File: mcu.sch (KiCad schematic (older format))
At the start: 75 parts, among them J11 RJ45_Shielded, J13 HR911105A, J2 RJ45_Shielded, U3 STM32F207VGT6, U4 MCP2562-E-P, U5 LAN8742A, Y1 Crystal_GND24

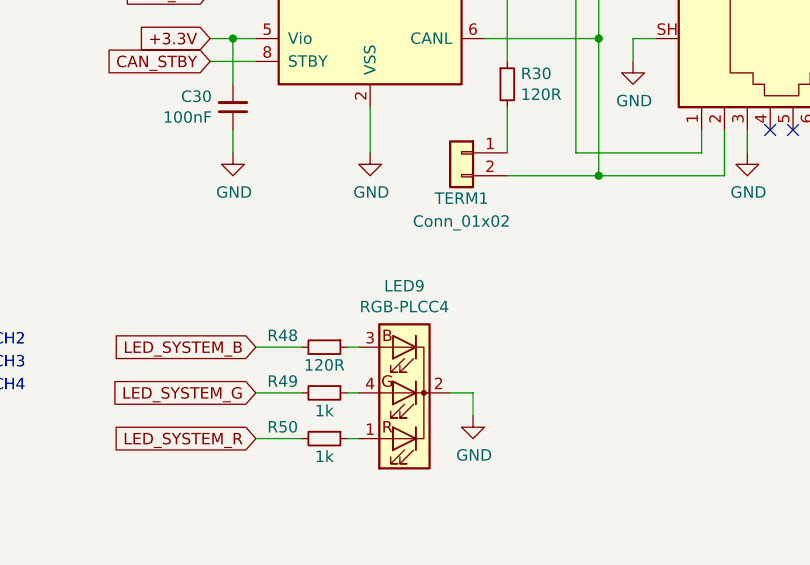
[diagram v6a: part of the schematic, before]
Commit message: PLCC-4 RGB LEDs LED9 and LED10 are the wrong parts (common cathode required, part is common anode and different input). Fix: source 0606 LEDs (metric 1616) - RD1616-63RGBC-C2CA or DL-PCB0606RGBC-C2. Require switching to Broadcom ASMB-TTF0-0A20B in next revision (uncommitted, can be configured as common cathode, available on Mouser)
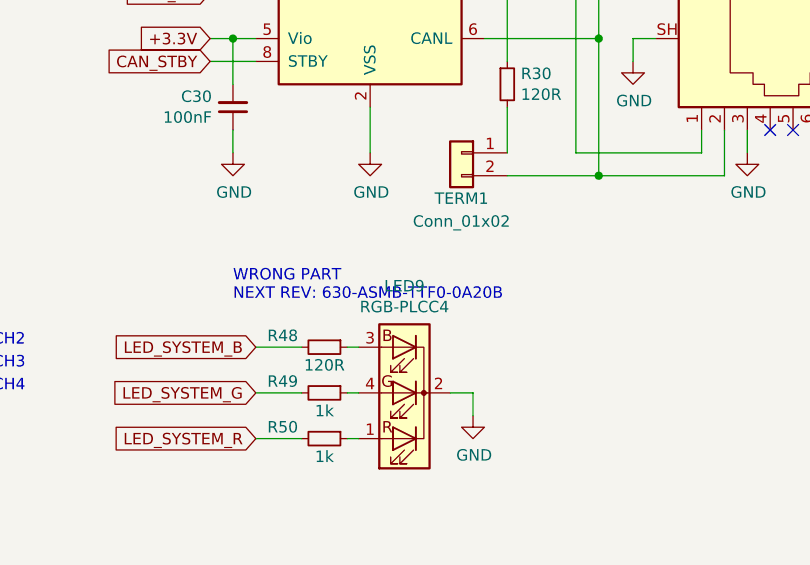
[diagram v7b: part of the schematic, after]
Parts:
- C15, C17, C18, C20, C24, C26, C27, C28, C30, C31, C34, C36, C37: box no (none) -> 2
- C19, C23, C32, C35: MPN 885012106011 -> C0603C225K9RACTU; Mouser 710-885012106011 -> 80-C0603C225K9R; box no (none) -> 4
- C2, C29: box no (none) -> 3
- C33: box no (none) -> 5
- J11, J2: box no (none) -> E; stock (X) -> X
- J13, RST1, TERM1, U4, Y1: box no (none) -> E
- LED9: MPN ASMB-KTF0-0A306 -> RD1616-63RGBC-C2CA or DL-PCB0606RGBC-C2; Mouser 630-ASMB-KTF0-0A306 -> 630-ASMB-KTF0-0A306 (WRONG PART)
- R19, R20, R22, R23, R24, R25, R26, R27: box no (none) -> 19
- R21, R35, R36, R42, R43, R44, R45, R46, R47, R49, R50, R51, R52, R53: box no (none) -> 21
- R28, R29, R31, R33: box no (none) -> 20
- R30, R48, R54: box no (none) -> 18
- U5: box no (none) -> E; stock (X) -> (none)
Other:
- note added: "WRONG PART\nNEXT REV: 630-ASMB-TTF0-0A20B"

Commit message: restored MCO1 = 25 MHz, PHY blinking pattern changed (SPEED on permanently, ACT fast blinking, RMII-RXDn activity) but TXEN only stays high for 6µs max. No SMI activity within 100ms after that.
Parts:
- C15, C17, C18, C19, C2, C20, C21, C22, C23, C24, C26, C27, C28, C29, C30, C31, C32, C33, C34, C35, C36, C37: symbol Device:C_Small -> panel_light_control-rescue:C_Small-Device
- J11, J2: symbol Connector:RJ45_Shielded -> panel_light_control-rescue:RJ45_Shielded-Connector
- L1: symbol Device:L -> panel_light_control-rescue:L-Device
- LED0, LED1, LED2, LED3, LED4, LED5, LED6, LED7, LED8: symbol Device:LED_Small -> panel_light_control-rescue:LED_Small-Device
- LED9: symbol Device:LED_RCBG -> panel_light_control-rescue:LED_RCBG-Device
- R19, R20, R21, R22, R23, R24, R25, R26, R27, R35, R36, R54: symbol Device:R -> panel_light_control-rescue:R-Device
- R28, R29, R30, R31, R32, R33, R34, R37, R38, R42, R43, R44, R45, R46, R47, R48, R49, R50, R51, R52, R53: symbol Device:R_Small -> panel_light_control-rescue:R_Small-Device
- RST1: symbol SamacSys_Parts:SKQYABE010 -> panel_light_control-rescue:SKQYABE010-SamacSys_Parts
- TERM1: symbol Connector_Generic:Conn_01x02 -> panel_light_control-rescue:Conn_01x02-Connector_Generic
- U3: symbol MCU_ST_STM32F2:STM32F207VGTx -> panel_light_control-rescue:STM32F207VGTx-MCU_ST_STM32F2
- U4: symbol Interface_CAN_LIN:MCP2562-E-P -> panel_light_control-rescue:MCP2562-E-P-Interface_CAN_LIN
- U5: symbol Interface_Ethernet:LAN8720A -> panel_light_control-rescue:LAN8720A-Interface_Ethernet
- Y1: symbol Device:Crystal_GND24 -> panel_light_control-rescue:Crystal_GND24-Device
